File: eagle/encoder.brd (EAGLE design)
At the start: 100 x 80 mm, 31 parts, among them IC1 LM339D, J1 SPI, U1 MCP42XXX, U2 ATMEGA328P

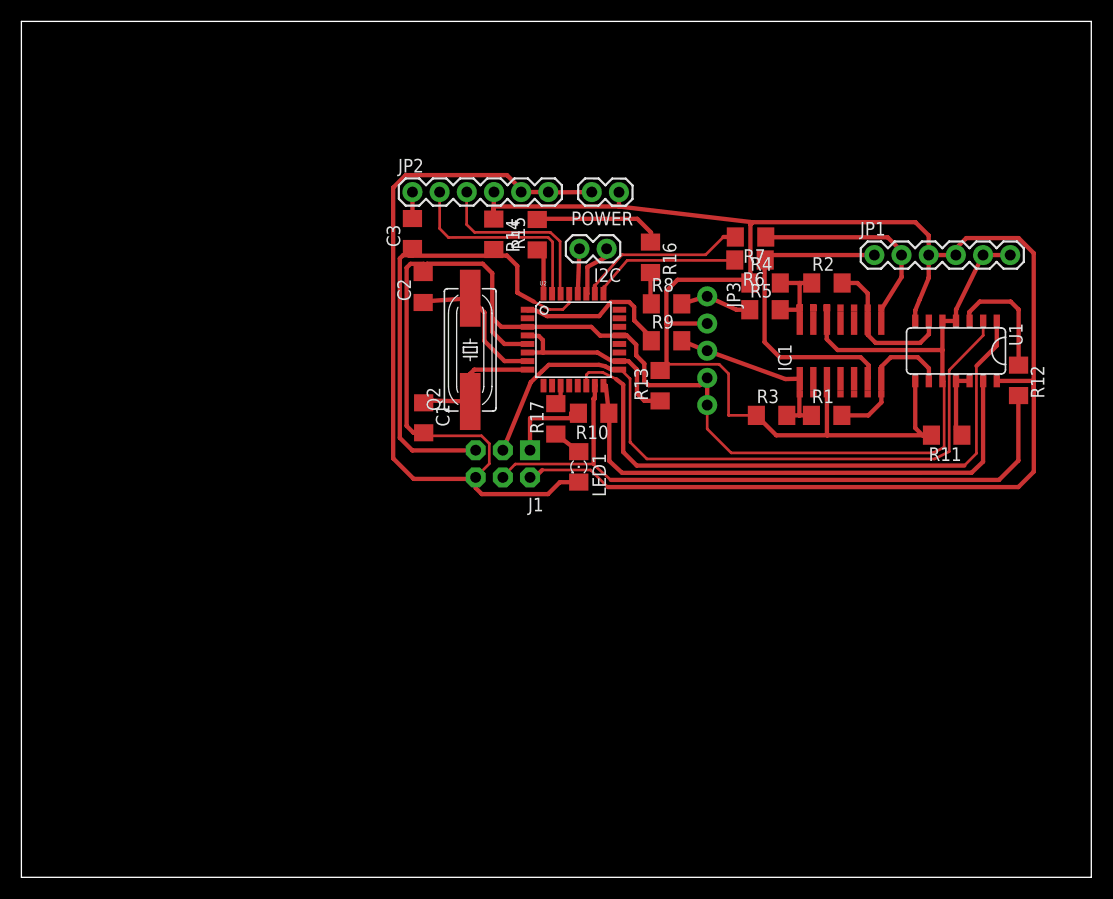
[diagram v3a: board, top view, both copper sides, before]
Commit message: Minor borad layout updates.
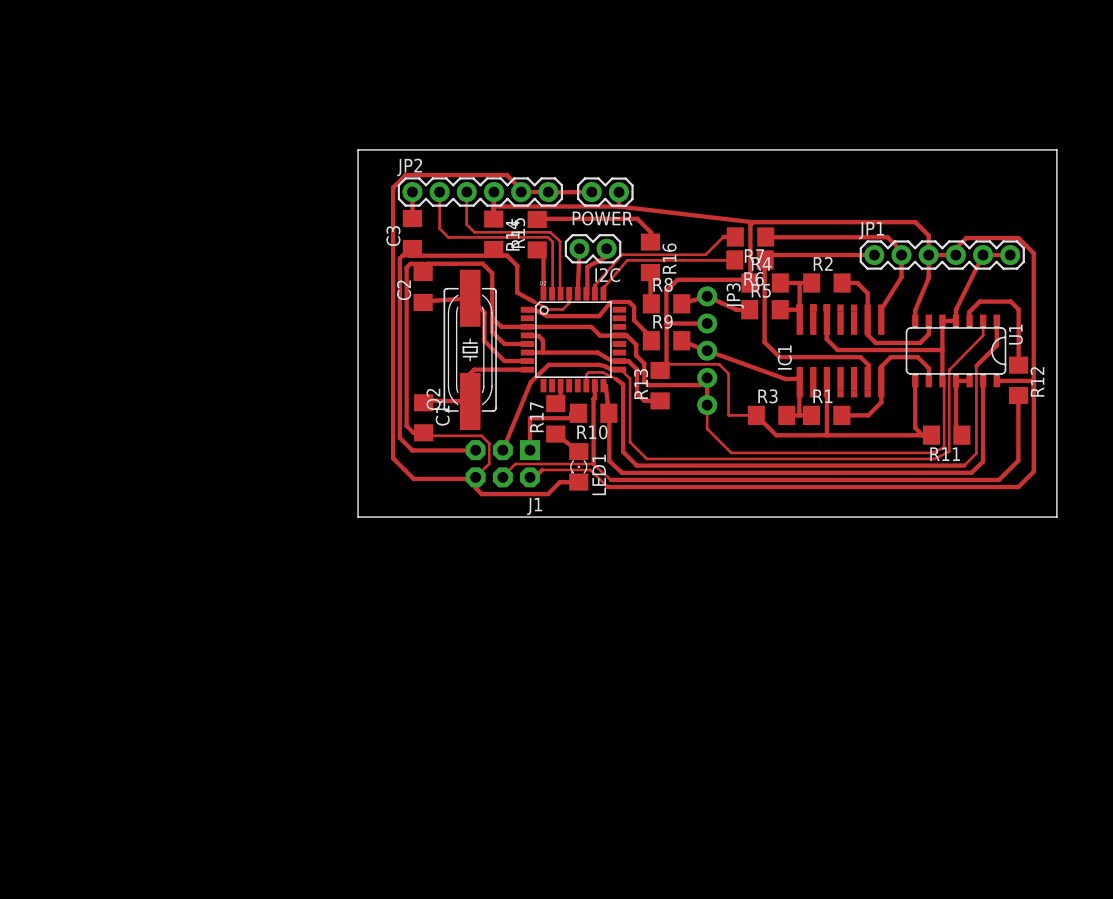
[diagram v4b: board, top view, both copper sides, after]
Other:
- board size 100 x 80 mm -> 65.3 x 34.3 mm
